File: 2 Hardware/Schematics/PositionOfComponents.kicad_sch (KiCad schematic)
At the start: 9 parts

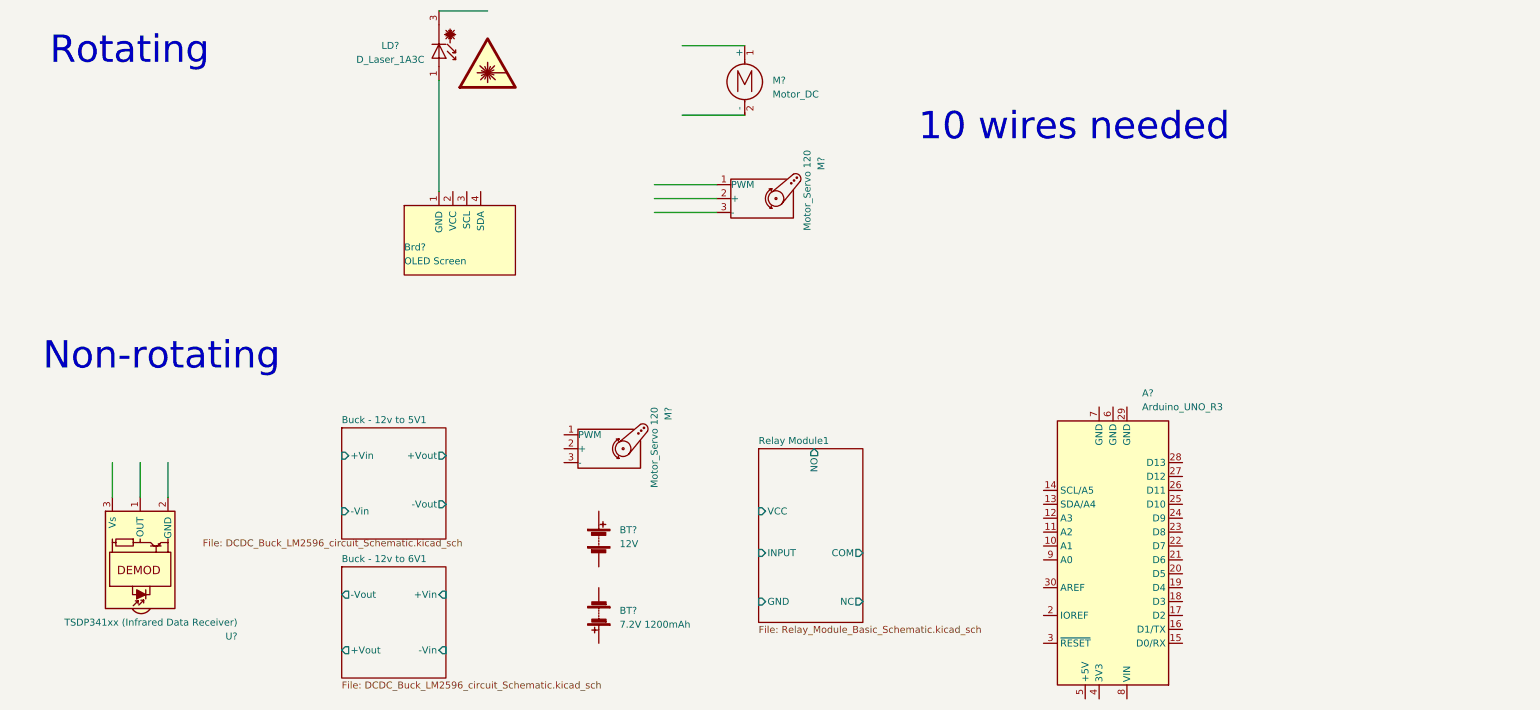
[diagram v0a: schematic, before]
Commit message: Have added the ESP-32 and reorginised the schematic
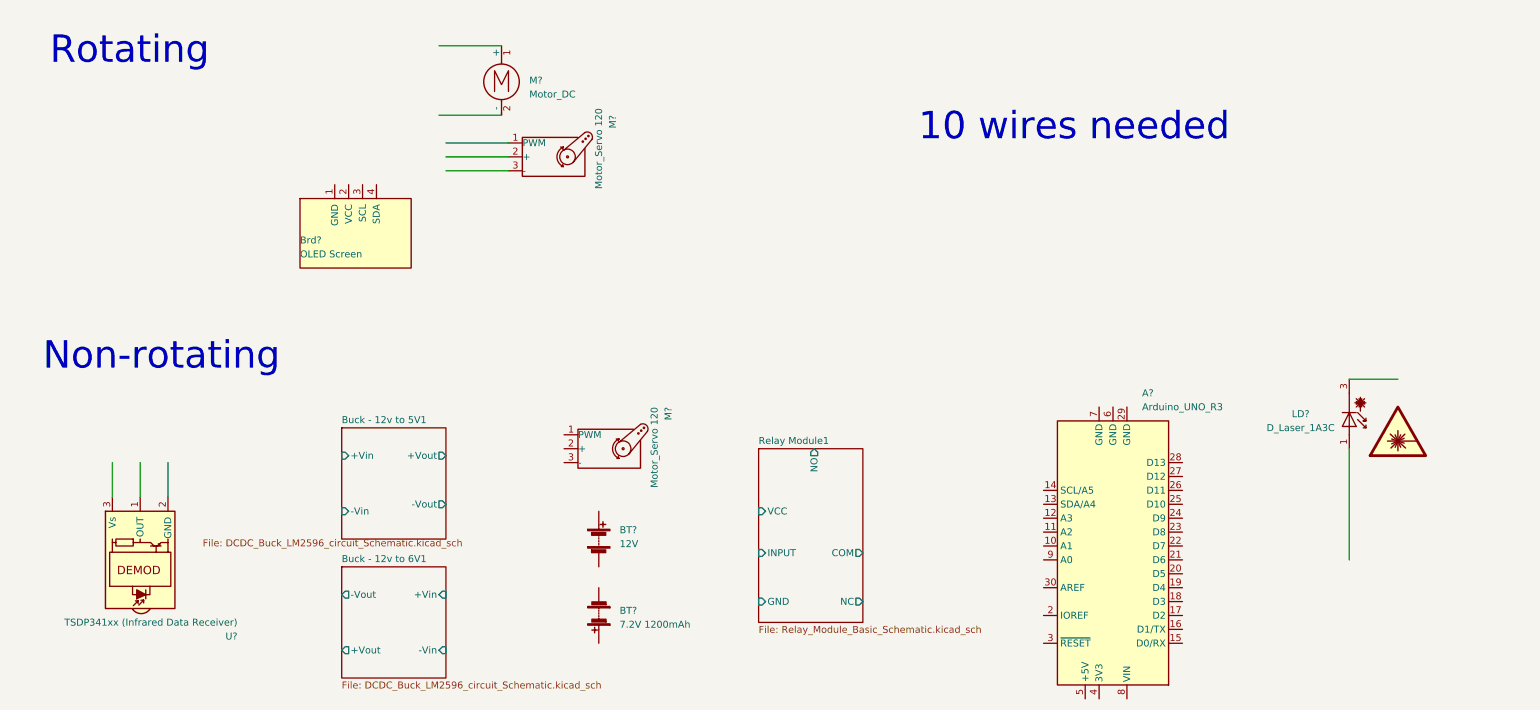
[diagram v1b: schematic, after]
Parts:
- removed LD?: D_Laser_1A3C, symbol Device:D_Laser_1A3C
- added LD?: D_Laser_1A3C, symbol Device:D_Laser_1A3C
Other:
- moved on the sheet: Brd?, M?
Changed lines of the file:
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@@
 (kicad_sch (version 20211123) (generator eeschema)
   (paper "A4")
-  (wire (pts (xy 146.05 46.99) (xy 134.62 46.99))
+  (wire (pts (xy 107.95 39.37) (xy 96.52 39.37))
     (stroke (width 0) (type default) (color 0 0 0 0))
   )
@@
     (stroke (width 0) (type default) (color 0 0 0 0))
   )
-  (wire (pts (xy 146.05 52.07) (xy 134.62 52.07))
-    (stroke (width 0) (type default) (color 0 0 0 0))
-  )
-  (wire (pts (xy 95.25 15.24) (xy 104.14 15.24))
+  (wire (pts (xy 107.95 44.45) (xy 96.52 44.45))
     (stroke (width 0) (type default) (color 0 0 0 0))
   )
@@
     (stroke (width 0) (type default) (color 0 0 0 0))
   )
-  (wire (pts (xy 151.13 21.59) (xy 139.7 21.59))
-    (stroke (width 0) (type default) (color 0 0 0 0))
-  )
-  (wire (pts (xy 134.62 49.53) (xy 146.05 49.53))
-    (stroke (width 0) (type default) (color 0 0 0 0))
-  )
-  (wire (pts (xy 95.25 27.94) (xy 95.25 48.26))
-    (stroke (width 0) (type default) (color 0 0 0 0))
-  )
-  (wire (pts (xy 139.7 34.29) (xy 151.13 34.29))
+  (wire (pts (xy 261.62 82.55) (xy 270.51 82.55))
+    (stroke (width 0) (type default) (color 0 0 0 0))
+  )
+  (wire (pts (xy 106.68 21.59) (xy 95.25 21.59))
+    (stroke (width 0) (type default) (color 0 0 0 0))
+  )
+  (wire (pts (xy 261.62 95.25) (xy 261.62 115.57))
+    (stroke (width 0) (type default) (color 0 0 0 0))
+  )
+  (wire (pts (xy 96.52 41.91) (xy 107.95 41.91))
+    (stroke (width 0) (type default) (color 0 0 0 0))
+  )
+  (wire (pts (xy 95.25 34.29) (xy 106.68 34.29))
     (stroke (width 0) (type default) (color 0 0 0 0))
   )
@@
     (pin "2")
   )
-  (symbol (lib_id "Motor:Motor_DC") (at 151.13 26.67 0) (unit 1)
-    (in_bom yes) (on_board yes) (fields_autoplaced)
-    (property "Reference" "M?" (id 0) (at 156.21 27.9399 0)
-      (effects (font (size 1.27 1.27)) (justify left))
-    )
-    (property "Value" "Motor_DC" (id 1) (at 156.21 30.4799 0)
-      (effects (font (size 1.27 1.27)) (justify left))
-    )
-    (property "Footprint" "" (id 2) (at 151.13 28.956 0)
-      (effects (font (size 1.27 1.27)) hide)
-    )
-    (property "Datasheet" "~" (id 3) (at 151.13 28.956 0)
+  (symbol (lib_id "Motor:Motor_DC") (at 106.68 26.67 0) (unit 1)
+    (in_bom yes) (on_board yes) (fields_autoplaced)
+    (property "Reference" "M?" (id 0) (at 111.76 27.9399 0)
+      (effects (font (size 1.27 1.27)) (justify left))
+    )
+    (property "Value" "Motor_DC" (id 1) (at 111.76 30.4799 0)
+      (effects (font (size 1.27 1.27)) (justify left))
+    )
+    (property "Footprint" "" (id 2) (at 106.68 28.956 0)
+      (effects (font (size 1.27 1.27)) hide)
+    )
+    (property "Datasheet" "~" (id 3) (at 106.68 28.956 0)
       (effects (font (size 1.27 1.27)) hide)
     )
@@
     (pin "3")
   )
-  (symbol (lib_id "Device:D_Laser_1A3C") (at 95.25 22.86 270) (unit 1)
-    (in_bom yes) (on_board yes)
-    (property "Reference" "LD?" (id 0) (at 86.36 21.59 90))
-    (property "Value" "D_Laser_1A3C" (id 1) (at 86.36 24.13 90))
-    (property "Footprint" "" (id 2) (at 94.615 20.32 0)
-      (effects (font (size 1.27 1.27)) hide)
-    )
-    (property "Datasheet" "~" (id 3) (at 90.17 23.622 0)
-      (effects (font (size 1.27 1.27)) hide)
-    )
-    (pin "1")
-    (pin "3")
-  )
-  (symbol (lib_id "Motor:Motor_Servo") (at 153.67 49.53 0) (unit 1)
-    (in_bom yes) (on_board yes)
-    (property "Reference" "M?" (id 0) (at 165.1 41.91 90)
-      (effects (font (size 1.27 1.27)) (justify right))
-    )
-    (property "Value" " Motor_Servo 120" (id 1) (at 162.56 40.64 90)
-      (effects (font (size 1.27 1.27)) (justify right))
-    )
-    (property "Footprint" "" (id 2) (at 153.67 54.356 0)
-      (effects (font (size 1.27 1.27)) hide)
-    )
-    (property "Datasheet" "https://www.ebay.co.uk/itm/265497022589?var=565305471806&_trkparms=amclksrc%3DITM%26aid%3D777008%26algo%3DPERSONAL.TOPIC%26ao%3D1%26asc%3D20220705100511%26meid%3D821d6b82bef041acaef308022d3ecea8%26pid%3D101524%26rk%3D1%26rkt%3D1%26itm%3D565305471806%26pmt%3D1%26noa%3D1%26pg%3D2380057%26algv%3DRecentlyViewedItemsV2%26brand%3DUnbranded&_trksid=p2380057.c101524.m146925&_trkparms=pageci%3A00132f18-fcc4-11ed-ad5c-7ec5643b6c91%7Cparentrq%3A5eaab6c01880acd89d2ad418ffe95f00%7Ciid%3A1" (id 3) (at 153.67 54.356 0)
-      (effects (font (size 1.27 1.27)) hide)
-    )
-    (pin "1")
-    (pin "2")
+  (symbol (lib_id "Graphic:SYM_LASER_Large") (at 270.51 91.44 0) (unit 1)
+    (in_bom yes) (on_board yes) (fields_autoplaced)
+    (property "Reference" "#SYM?" (id 0) (at 270.51 86.36 0)
+      (effects (font (size 1.27 1.27)) hide)
+    )
+    (property "Value" "SYM_LASER_Large" (id 1) (at 270.51 98.171 0)
+      (effects (font (size 1.27 1.27)) hide)
+    )
+    (property "Footprint" "" (id 2) (at 270.256 95.885 0)
+      (effects (font (size 1.27 1.27)) hide)
+    )
+    (property "Datasheet" "~" (id 3) (at 271.272 96.52 0)
+      (effects (font (size 1.27 1.27)) hide)
+    )
+  )
+  (symbol (lib_id "Motor:Motor_Servo") (at 115.57 41.91 0) (unit 1)
+    (in_bom yes) (on_board yes)
+    (property "Reference" "M?" (id 0) (at 127 34.29 90)
+      (effects (font (size 1.27 1.27)) (justify right))
+    )
+    (property "Value" " Motor_Servo 120" (id 1) (at 124.46 33.02 90)
+      (effects (font (size 1.27 1.27)) (justify right))
+    )
+    (property "Footprint" "" (id 2) (at 115.57 46.736 0)
+      (effects (font (size 1.27 1.27)) hide)
+    )
+    (property "Datasheet" "https://www.ebay.co.uk/itm/265497022589?var=565305471806&_trkparms=amclksrc%3DITM%26aid%3D777008%26algo%3DPERSONAL.TOPIC%26ao%3D1%26asc%3D20220705100511%26meid%3D821d6b82bef041acaef308022d3ecea8%26pid%3D101524%26rk%3D1%26rkt%3D1%26itm%3D565305471806%26pmt%3D1%26noa%3D1%26pg%3D2380057%26algv%3DRecentlyViewedItemsV2%26brand%3DUnbranded&_trksid=p2380057.c101524.m146925&_trkparms=pageci%3A00132f18-fcc4-11ed-ad5c-7ec5643b6c91%7Cparentrq%3A5eaab6c01880acd89d2ad418ffe95f00%7Ciid%3A1" (id 3) (at 115.57 46.736 0)
+      (effects (font (size 1.27 1.27)) hide)
+    )
+    (pin "1")
+    (pin "2")
+    (pin "3")
+  )
+  (symbol (lib_id "Device:D_Laser_1A3C") (at 261.62 90.17 270) (unit 1)
+    (in_bom yes) (on_board yes)
+    (property "Reference" "LD?" (id 0) (at 252.73 88.9 90))
+    (property "Value" "D_Laser_1A3C" (id 1) (at 252.73 91.44 90))
+    (property "Footprint" "" (id 2) (at 260.985 87.63 0)
+      (effects (font (size 1.27 1.27)) hide)
+    )
+    (property "Datasheet" "~" (id 3) (at 256.54 90.932 0)
+      (effects (font (size 1.27 1.27)) hide)
+    )
+    (pin "1")
     (pin "3")
   )
@@
     (pin "2")
   )
-  (symbol (lib_id "Graphic:SYM_LASER_Large") (at 104.14 24.13 0) (unit 1)
-    (in_bom yes) (on_board yes) (fields_autoplaced)
-    (property "Reference" "#SYM?" (id 0) (at 104.14 19.05 0)
-      (effects (font (size 1.27 1.27)) hide)
-    )
-    (property "Value" "SYM_LASER_Large" (id 1) (at 104.14 30.861 0)
-      (effects (font (size 1.27 1.27)) hide)
-    )
-    (property "Footprint" "" (id 2) (at 103.886 28.575 0)
-      (effects (font (size 1.27 1.27)) hide)
-    )
-    (property "Datasheet" "~" (id 3) (at 104.902 29.21 0)
-      (effects (font (size 1.27 1.27)) hide)
-    )
-  )
-  (symbol (lib_id "Custom_Lib:0.96_OLED_SSD1306") (at 99.06 57.15 0) (unit 1)
-    (in_bom yes) (on_board yes)
-    (property "Reference" "Brd?" (id 0) (at 88.9 58.42 0)
-      (effects (font (size 1.27 1.27)) (justify left))
-    )
-    (property "Value" "OLED Screen" (id 1) (at 88.9 60.96 0)
-      (effects (font (size 1.27 1.27)) (justify left))
-    )
-    (property "Footprint" "Custom_lib:0.96_Oled_SSD1306" (id 2) (at 99.06 67.31 0)
-      (effects (font (size 1.27 1.27)) hide)
-    )
-    (property "Datasheet" "https://www.amazon.co.uk/gp/product/B074N9VLZX/ref=ppx_yo_dt_b_search_asin_title?ie=UTF8&psc=1" (id 3) (at 108.585 64.77 0)
-      (effects (font (size 1.27 1.27)) hide)
-    )
+  (symbol (lib_id "Custom_Lib:0.96_OLED_SSD1306") (at 80.01 55.88 0) (unit 1)
+    (in_bom yes) (on_board yes)
+    (property "Reference" "Brd?" (id 0) (at 69.85 57.15 0)
+      (effects (font (size 1.27 1.27)) (justify left))
+    )
+    (property "Value" "OLED Screen" (id 1) (at 69.85 59.69 0)
+      (effects (font (size 1.27 1.27)) (justify left))
+    )
+    (property "Footprint" "Custom_lib:0.96_Oled_SSD1306" (id 2) (at 80.01 66.04 0)
+      (effects (font (size 1.27 1.27)) hide)
+    )
+    (property "Datasheet" "https://www.amazon.co.uk/gp/product/B074N9VLZX/ref=ppx_yo_dt_b_search_asin_title?ie=UTF8&psc=1" (id 3) (at 89.535 63.5 0)
+      (effects (font (size 1.27 1.27)) hide)
+    )

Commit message: Added gitignre, changes (minor) to schematic, changes to horizontal model (WithWheels) and general repo cleanup
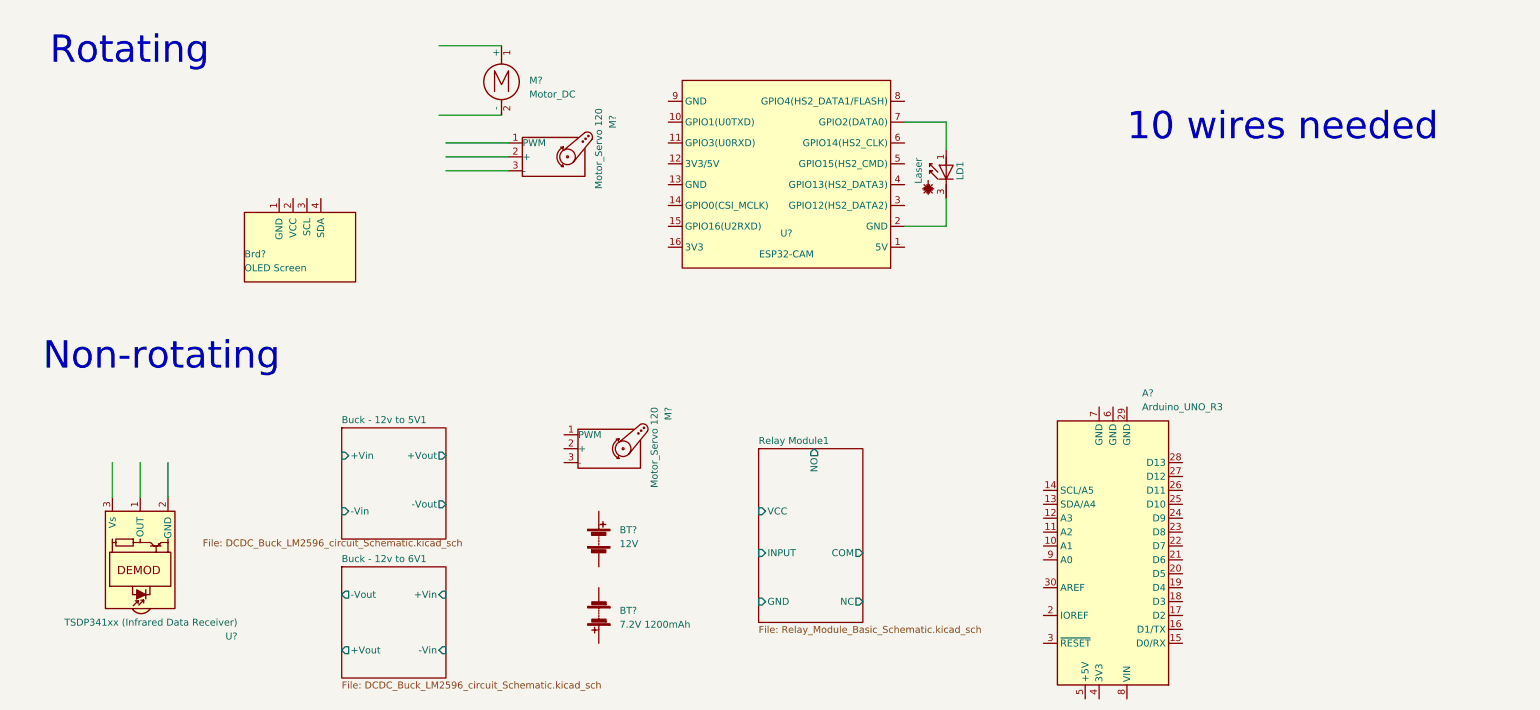
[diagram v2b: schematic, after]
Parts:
- removed LD?: D_Laser_1A3C, symbol Device:D_Laser_1A3C
- added LD1: Laser, symbol Device:D_Laser_1A3C
- added U?: ESP32-CAM, symbol Custom_Lib:ESP32-CAM
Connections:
- new net: LD1.1 (A), U?.7 (GPIO2(DATA0))
- new net: LD1.3 (K), U?.2 (GND)
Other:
- moved on the sheet: Brd?
